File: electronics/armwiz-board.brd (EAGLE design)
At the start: 99.1 x 51.5 mm, 100 parts, among them J1 MICRO-SDCARD-CONNECTOR-330006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, J15 Cortex Debug, J16 ST-Link v2, J2 CORTEX_DEBUGSMD, U1 STM32F10XRXT6, U4 MIC5219-3.3V, X1 FH12-12S-1S, Y3 32.768kHz

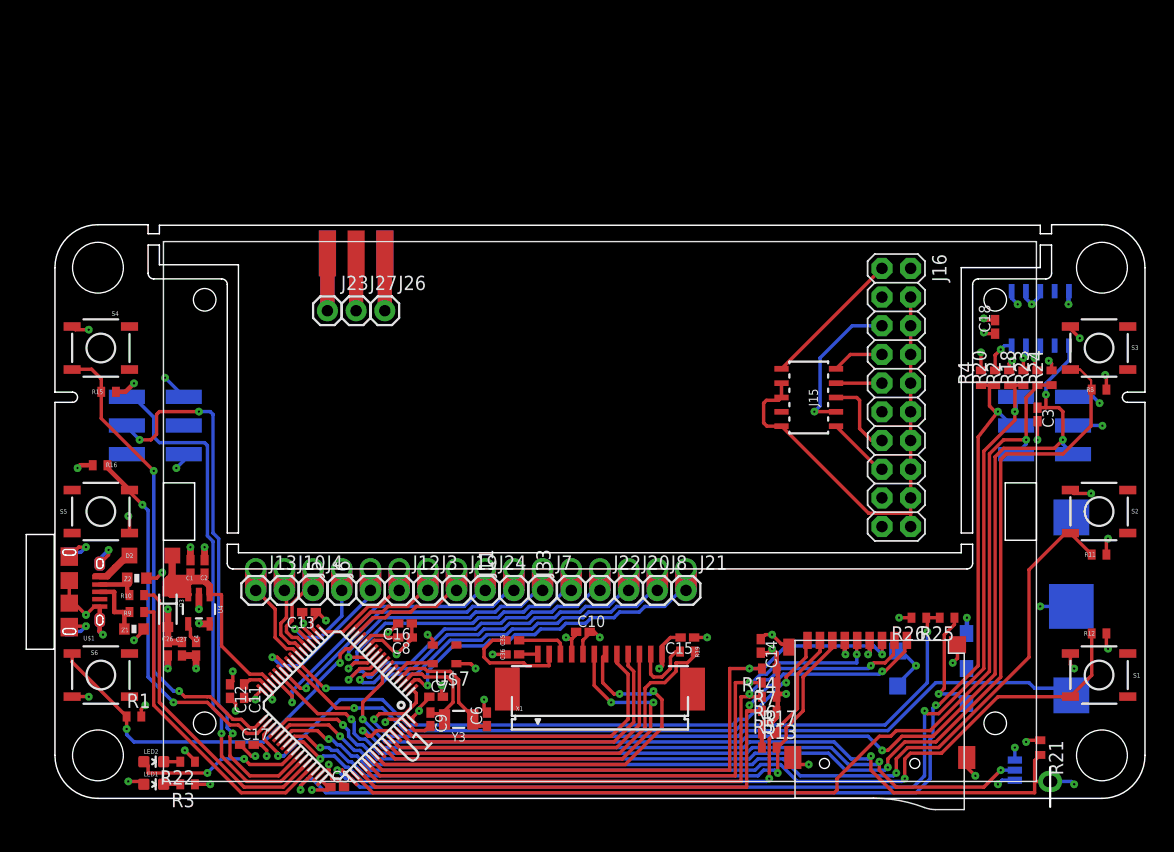
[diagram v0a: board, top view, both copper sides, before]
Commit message: Changed to a metric layout. Moved to a 7x2 2.0mm module connector.
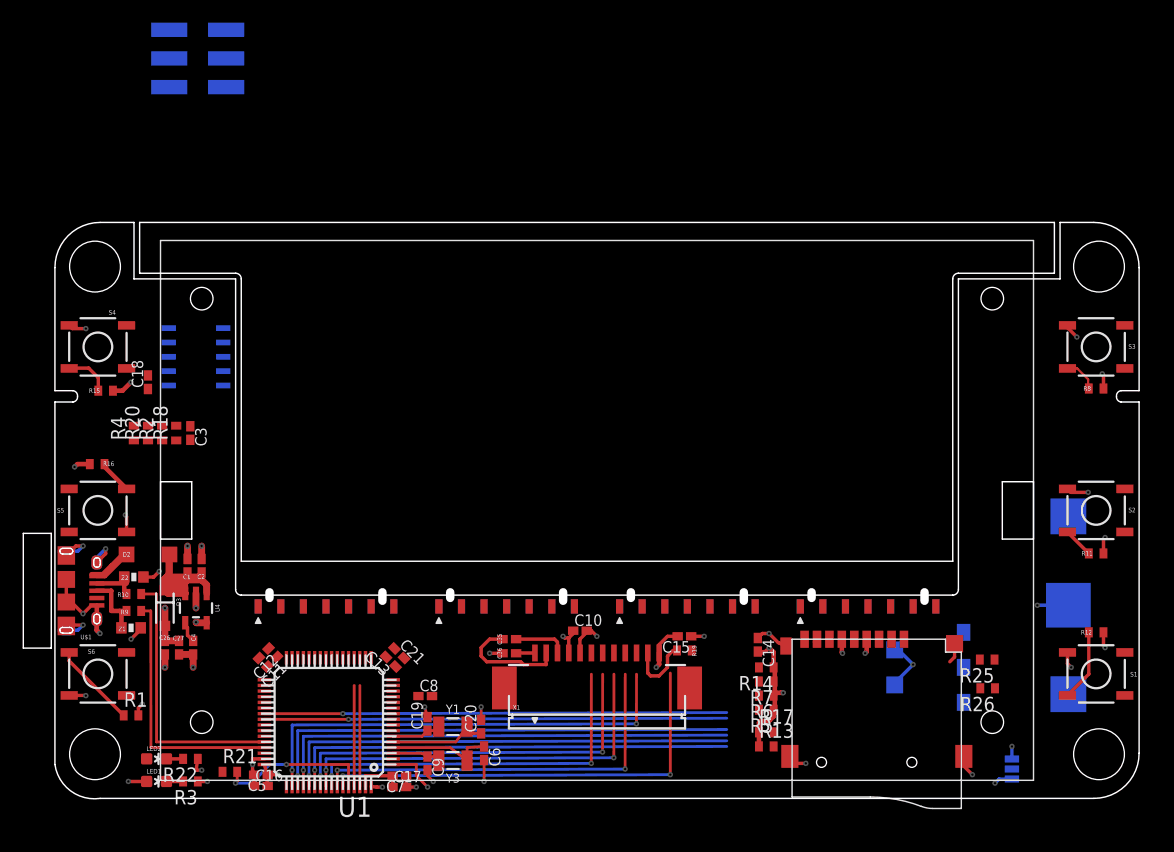
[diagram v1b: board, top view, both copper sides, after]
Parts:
- removed J$1: SMA_EDGE, SparkFun-Connectors:SMA-EDGE
- removed J10, J11, J12, J13, J19, J20, J21, J22, J23, J24, J26, J27, J3, J33, J4, J5, J6, J7, J8: (no value), SparkFun-Connectors:1X01
- removed J14: (no value), PaxInstruments-Connectors:CONNECTORS_2X3_SMT_POSTS_T400
- removed J15: Cortex Debug, SparkFun-Connectors:SAMTECH_FTSH-105-01
- removed J16: ST-Link v2, SparkFun-Connectors:2X10
- removed J17, J18: (no value), SparkFun-Connectors:1X01NS-KIT
- removed R23: 100R, resistor:R0402
- removed R24: 10K, resistor:R0402
- added C19, C20: 8pF, resistor:C0402K
- added C21: 10uF, resistor:C0402K
- added U$4, U$8, U$9: PAX_MODULE, PaxInstruments-Connectors:7X2_2MM_EDGE
- added Y1: 32.768kHz, SparkFun-FreqCtrl:CRYSTAL-SMD-3.2X1.5MM
- U$7: value ASDM1-16.000MHz-LCT -> PAX_MODULE; device crystal:ASE -> PaxInstruments-Connectors:7X2_2MM_EDGE
- moved U$6 117.1 mm to (78.0, 120.7)
- moved C18 75.2 mm to (8.24, 36.9)
- moved R18 75.2 mm to (10.7, 32.4)
- moved R2 75.2 mm to (9.49, 32.4)
- moved R20 75.2 mm to (8.24, 32.4)
- moved R4 75.2 mm to (6.99, 32.4)
- moved C3 75.0 mm to (12.0, 32.4)
- moved J2 74.8 mm to (12.5, 39.1), turned to 270 degrees
- moved R21 71.8 mm to (15.5, 2.35), turned to 0 degrees
- moved J25 32.7 mm to (12.6, 65.5)
- moved C16 19.2 mm to (18.2, 1.10), turned to 0 degrees
- moved C17 14.0 mm to (30.5, 1.00)
- moved R26 8.73 mm to (82.6, 9.75)
- moved C13 8.47 mm to (29.7, 12.1), turned to 135 degrees
- moved C7 7.72 mm to (30.5, 2.00), turned to 180 degrees
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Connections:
- net BOOT1 renamed (BOOT1)
- net MISO3 renamed PB4
- net MOSI3 renamed LCD_MOSI_(SPI3_MOSI)
- net RTC1 renamed RTC_OSC_IN
- net RTC2 renamed RTC_OSC_OUT
- net SCK3 renamed LCD_SCK_(SPI3_SCK)
- net SW_PWR renamed SW_PWR_(SYS_WKUP)
- removed net AD_GND: J15.3, J15.5, J15.9, J16.10, J16.12, J16.14, J16.16, J16.18, J16.20, J16.4, J16.6, J16.8
- removed net AD_NRST: J15.10, J16.15
- removed net AD_SWDCLK: J15.4, J16.9
- removed net AD_SWDIO: J15.2, J16.7
- removed net AD_SWO: J15.6, J16.13
- removed net AD_TDI: J15.8, J16.5
- removed net AD_VCC: J15.1, J16.1
- removed net LCD_A0: U1.62, X1.8
- removed net LCD_BL: R19.2, U1.58
- removed net LCD_CS: U1.59, X1.10
- removed net LCD_RST: U1.61, X1.9
- removed net MISO1: J10.1, U1.22
- removed net MOSI1: J13.1, U1.23
- removed net N$12: J2.6, R23.2
- removed net N$14: J$1.GND@1, J$1.GND@3, J26.1
- removed net N$15: J$1.GND@0, J$1.GND@2, J23.1
- removed net N$20: J$1.SIG, J27.1
- removed net PA2: J3.1, U1.16
- removed net PA3: J12.1, U1.17
- removed net PA4: J5.1, U1.20
- removed net PB10: J24.1, U1.29
- removed net PC0: J20.1, U1.8
- removed net PC1: J22.1, U1.9
- removed net PC13: J21.1, U1.2
- removed net SCLK1: J4.1, U1.21
- removed net SWDCLK: J14.2, R18.1, R2.1, U1.49
- removed net SWO: J14.6, R23.1, R24.1, U1.50
- removed net USB+: R9.2, U1.45
- removed net USB-: R10.2, U1.44
- removed net VBAT2: R25.2, R26.1, U1.25
- new net 12C1_SDA: U1.59
- new net CAN_RX: U$4.P$4, U$7.P$4, U$8.P$4, U$9.P$4, U1.61
- new net CAN_TX: U$4.P$6, U$7.P$6, U$8.P$6, U$9.P$6, U1.62
- new net GPIO_(SPI1_NSS): U$8.P$9, U1.20
- new net GPIO_(SPI2_NSS): U$4.P$9, U1.33
- new net I2C1_SCL: U$4.P$10, U$7.P$10, U1.58
- new net I2C1_SDA: U$4.P$8, U$7.P$8
- new net I2C2_SCL: U$8.P$10, U$9.P$10, U1.29
- new net I2C2_SDA: U$8.P$8, U$9.P$8, U1.30
- new net LCD_A0_(GPIO): U1.9, X1.8
- new net LCD_BL_(GPIO): R19.2, U1.8
- new net LCD_CS_(SPI3_NSS): U1.50, X1.10
- new net LCD_RST_(GPIO): U1.2, X1.9
- new net LED2: LED2.A
- new net N$51: U$8.P$11
- new net N$52: U$8.P$13
- new net N$57: U$4.P$11
- new net N$58: U$4.P$13
- new net N$68: U$7.P$9
- new net N$69: U$7.P$11
- new net N$70: U$7.P$13
- new net N$74: U$9.P$9
- new net N$75: U$9.P$11
- new net N$76: U$9.P$13
- new net OSC_OUT: C19.1, U1.6, Y1.P$1
- new net PC5: U1.25
- new net PC6: U1.37
- new net PC7: U1.38
- new net SPI1_MISO: U$8.P$5, U$9.P$5, U1.22
- new net SPI1_MOSI: U$8.P$3, U$9.P$3, U1.23
- new net SPI1_SCK: U$8.P$7, U$9.P$7, U1.21
- new net SPI2_MISO: U$4.P$5, U$7.P$5, U1.35
- new net SPI2_MOSI: U$4.P$3, U$7.P$3, U1.36
- new net SPI2_SCK: U$4.P$7, U$7.P$7, U1.34
- new net SWCLK: R18.1, R2.1, U1.49
- new net USART2_RX: U$4.P$12, U$7.P$12, U$8.P$12, U$9.P$12, U1.17
- new net USART2_TX: U$4.P$14, U$7.P$14, U$8.P$14, U$9.P$14, U1.16
- new net USB_DM: R10.2, U1.44
- new net USB_DP: R9.2, U1.45
- new net VBAT_1/2: R25.2, R26.1
- net 3.3V: now also C21.2, U$4.P$1, U$7.P$1, U$8.P$1, U$9.P$1; no longer J14.1, J18.1, R24.2, U$7.4
- net BOOT0: no longer J17.1
- net GND: now also C19.2, C20.2, C21.1, U$4.P$2, U$7.P$2, U$8.P$2, U$9.P$2; no longer J14.3, U$7.2
- net NRST: no longer J14.5
- net OSC_IN: now also C20.1, Y1.P$2; no longer U$7.3
- net PA1: no longer J19.1
- net PA8: no longer LED2.A
- net PB0: no longer J6.1
- net PB1: no longer J11.1
- net PC2: no longer J33.1
- net PC3: no longer J7.1
- net PC4: no longer J8.1
- net SD_DETECT: no longer U1.35
- net SWDIO: no longer J14.4
- net SW_A: no longer U1.36
- net SW_B: no longer U1.37
- net SW_C: no longer U1.38
- net SW_D: no longer U1.33
- net SW_E: no longer U1.34
- net VBUS: no longer U1.30
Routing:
- net NRST: track 104.8 -> 0.00 mm, vias 4 -> 0
- net SW_A: track 106.1 -> 3.07 mm, vias 2 -> 0
- net SWDIO: track 100.9 -> 0.00 mm, vias 3 -> 0
- net SWDCLK: track 96.4 -> 0.00 mm, vias 3 -> 0
- net SWO: track 92.8 -> 0.00 mm, vias 1 -> 0
- net SW_B: track 89.8 -> 2.69 mm, vias 2 -> 0
- net SW_C: track 83.0 -> 6.37 mm, vias 2 -> 0
- net (BOOT1): track 71.7 -> 0.00 mm, vias 3 -> 0
- net VBAT2: track 67.7 -> 0.00 mm, vias 2 -> 0
- net RTC_BAT: track 70.6 -> 4.46 mm
- net BOOT0: track 71.6 -> 13.7 mm
- net SD_DETECT: track 57.2 -> 0.00 mm, vias 2 -> 0
- net USART1_TX: track 48.9 -> 0.00 mm, vias 3 -> 0
- net USART1_RX: track 46.8 -> 0.00 mm, vias 1 -> 0
- net AD_GND: track 41.5 -> 0.00 mm
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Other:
- board size 99.1 x 51.5 mm -> 98.8 x 51 mm

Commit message: Updated board with new Pax Instruments library parts.
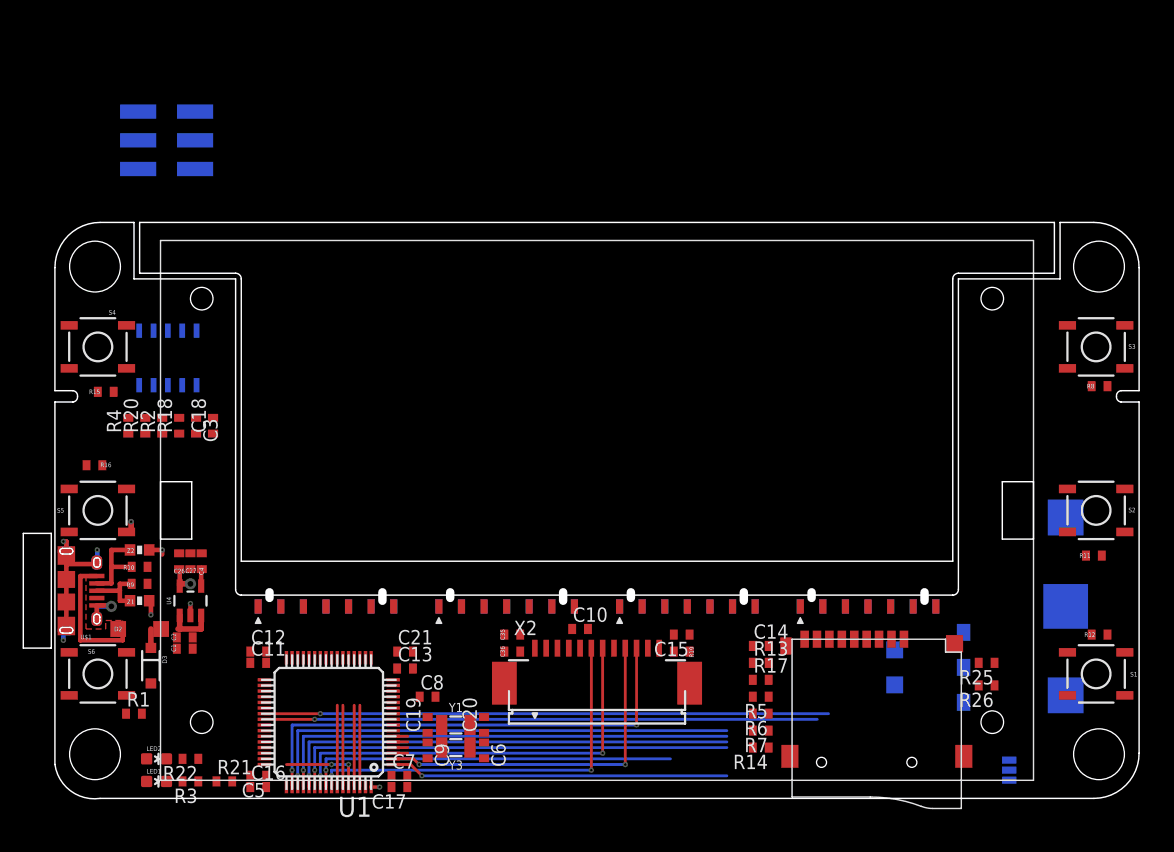
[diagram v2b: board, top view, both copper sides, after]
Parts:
- removed U$4, U$7, U$8, U$9: PAX_MODULE, PaxInstruments-Connectors:7X2_2MM_EDGE
- removed X1: FH12-12S-1S, PaxInstrument-T400:FH12-12S-1SH
- added MODULE1, MODULE2, MODULE3, MODULE4: PI-module-female, PaxInstruments-Connectors:M07X2_2MM_EDGE
- added X2: M12_BOTTOM_CONTACTS_FPC_1MM, PaxInstruments-Connectors:FPC_12P_1MM
- C1, C10, C11, C12, C13, C14, C15, C16, C17, C18, C19, C2, C20, C21, C26, C27, C3, C35, C36, C4, C5, C6, C7, C8, C9: device resistor:C0402K -> PaxInstruments-Capacitors:C0402
- J1: value MICRO-SDCARD-CONNECTOR-3300060P1 -> MICROSD; device PaxInstrument-T400:9P-SMD-W-RING -> PaxInstruments-Connectors:MICROSD_1
- R1, R11, R12, R15, R16, R8: value 10k -> 10K; device resistor:R0402 -> PaxInstruments-Resistors:R0402
- R10, R13, R14, R17, R18, R19, R2, R20, R21, R22, R25, R26, R3, R4, R5, R6, R7, R9: device resistor:R0402 -> PaxInstruments-Resistors:R0402
- moved U$6 59.8 mm to (81.3, 61.0)
- moved J25 7.75 mm to (9.89, 58.3)
- moved C26 7.75 mm to (11.0, 21.0), turned to 90 degrees
- moved C27 7.72 mm to (12.0, 21.0), turned to 90 degrees
- moved C4 7.69 mm to (13.0, 21.0), turned to 90 degrees
- moved R13 7.42 mm to (62.5, 12.0)
- moved C1 7.35 mm to (11.5, 13.2), turned to 0 degrees
- moved R14 7.12 mm to (62.5, 4.50)
- moved C18 6.93 mm to (14.0, 33.0)
- moved D2 6.64 mm to (7.50, 15.0)
- moved C2 6.52 mm to (11.5, 14.2), turned to 0 degrees
- moved D3 5.25 mm to (8.50, 11.8)
- moved R17 4.68 mm to (62.5, 10.5)
- moved R7 4.38 mm to (62.5, 6.00)
- moved Z1 2.52 mm to (7.50, 17.5)
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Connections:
- removed net 12C1_SDA: U1.59
- removed net N$52: U$8.P$13
- removed net N$58: U$4.P$13
- removed net N$70: U$7.P$13
- removed net N$76: U$9.P$13
- removed net PB4: U1.56
- new net PC0: U1.8
- net 3.3V: now also C11.1, C12.1, C13.1, C16.1, C17.1, C21.1, C26.2, C27.2, C8.1, MODULE1.P$1, MODULE2.P$1, MODULE3.P$1, MODULE4.P$1, R13.2, R14.2, R17.2, R5.2, R6.2, R7.2, X2.12, X2.5; no longer C11.2, C12.2, C13.2, C16.2, C17.2, C21.2, C26.1, C27.1, C8.2, R13.1, R14.1, R17.1, R5.1, R6.1, R7.1, U$4.P$1, U$7.P$1, U$8.P$1, U$9.P$1, X1.12, X1.5
- net CAN_RX: now also MODULE1.P$4, MODULE2.P$4, MODULE3.P$4, MODULE4.P$4; no longer U$4.P$4, U$7.P$4, U$8.P$4, U$9.P$4
- net CAN_TX: now also MODULE1.P$6, MODULE2.P$6, MODULE3.P$6, MODULE4.P$6; no longer U$4.P$6, U$7.P$6, U$8.P$6, U$9.P$6
- net GND: now also C1.1, C11.2, C12.2, C13.2, C16.2, C17.2, C2.1, C21.2, C26.1, C27.1, C8.2, MODULE1.P$13, MODULE1.P$2, MODULE2.P$13, MODULE2.P$2, MODULE3.P$13, MODULE3.P$2, MODULE4.P$13, MODULE4.P$2, R1.1, R22.2, R3.2, X2.4; no longer C1.2, C11.1, C12.1, C13.1, C16.1, C17.1, C2.2, C21.1, C26.2, C27.2, C8.1, R1.2, R22.1, R3.1, U$4.P$2, U$7.P$2, U$8.P$2, U$9.P$2, X1.4
- net GPIO_(SPI1_NSS): now also MODULE3.P$9; no longer U$8.P$9
- net GPIO_(SPI2_NSS): now also MODULE1.P$9; no longer U$4.P$9
- net I2C1_SCL: now also MODULE1.P$10, MODULE2.P$10; no longer U$4.P$10, U$7.P$10
- net I2C1_SDA: now also MODULE1.P$8, MODULE2.P$8, U1.59; no longer U$4.P$8, U$7.P$8
- net I2C2_SCL: now also MODULE3.P$10, MODULE4.P$10; no longer U$8.P$10, U$9.P$10
- net I2C2_SDA: now also MODULE3.P$8, MODULE4.P$8; no longer U$8.P$8, U$9.P$8
- net LCD_A0_(GPIO): now also X2.8; no longer X1.8
- net LCD_BL_(GPIO): now also U1.56; no longer U1.8
- net LCD_CS_(SPI3_NSS): now also X2.10; no longer X1.10
- net LCD_MOSI_(SPI3_MOSI): now also X2.6; no longer X1.6
- net LCD_RST_(GPIO): now also X2.9; no longer X1.9
- net LCD_SCK_(SPI3_SCK): now also X2.7; no longer X1.7
- net N$11: now also R22.1; no longer R22.2
- net N$37: now also X2.3; no longer X1.3
- net N$38: now also X2.2; no longer X1.2
- net N$39: now also X2.1; no longer X1.1
- net N$4: now also X2.11; no longer X1.11
- net N$51: now also MODULE3.P$11; no longer U$8.P$11
- net N$57: now also MODULE1.P$11; no longer U$4.P$11
- net N$68: now also MODULE2.P$9; no longer U$7.P$9
- net N$69: now also MODULE2.P$11; no longer U$7.P$11
- net N$7: now also R3.1; no longer R3.2
- net N$74: now also MODULE4.P$9; no longer U$9.P$9
- net N$75: now also MODULE4.P$11; no longer U$9.P$11
- net SDIO_CLK: now also R7.1; no longer R7.2
- net SDIO_CMD: now also R14.1; no longer R14.2
- net SDIO_D0: now also R13.1; no longer R13.2
- net SDIO_D1: now also R17.1; no longer R17.2
- net SDIO_D2: now also R5.1; no longer R5.2
- net SDIO_D3: now also R6.1; no longer R6.2
- net SPI1_MISO: now also MODULE3.P$5, MODULE4.P$5; no longer U$8.P$5, U$9.P$5
- net SPI1_MOSI: now also MODULE3.P$3, MODULE4.P$3; no longer U$8.P$3, U$9.P$3
- net SPI1_SCK: now also MODULE3.P$7, MODULE4.P$7; no longer U$8.P$7, U$9.P$7
- net SPI2_MISO: now also MODULE1.P$5, MODULE2.P$5; no longer U$4.P$5, U$7.P$5
- net SPI2_MOSI: now also MODULE1.P$3, MODULE2.P$3; no longer U$4.P$3, U$7.P$3
- net SPI2_SCK: now also MODULE1.P$7, MODULE2.P$7; no longer U$4.P$7, U$7.P$7
- net SW_PWR_(SYS_WKUP): now also R1.2; no longer R1.1
- net USART2_RX: now also MODULE1.P$12, MODULE2.P$12, MODULE3.P$12, MODULE4.P$12; no longer U$4.P$12, U$7.P$12, U$8.P$12, U$9.P$12
- net USART2_TX: now also MODULE1.P$14, MODULE2.P$14, MODULE3.P$14, MODULE4.P$14; no longer U$4.P$14, U$7.P$14, U$8.P$14, U$9.P$14
- net VBUS: now also C1.2, C2.2; no longer C1.1, C2.1
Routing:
- net GND: track 78.3 -> 24.3 mm, vias 35 -> 8
- net 3.3V: track 44.7 -> 3.35 mm, vias 18 -> 2
- net 12C1_SDA: track 38.9 -> 0.00 mm, vias 2 -> 0
- net PB4: track 35.3 -> 0.00 mm, vias 2 -> 0
- net LCD_BL_(GPIO): track 0.00 -> 33.0 mm, vias 0 -> 1
- net LCD_RST_(GPIO): track 0.01 -> 31.1 mm, vias 0 -> 2
- net I2C1_SCL: track 35.3 -> 7.20 mm, vias 2 -> 0
- net RTC_BAT: track 4.46 -> 30.0 mm
- net USB_DM: track 24.0 -> 0.00 mm
- net USB_DP: track 23.0 -> 0.00 mm
- net VBUS: track 25.4 -> 6.12 mm
- net N$38: track 10.1 -> 0.00 mm
- net SDIO_D0: track 41.1 -> 50.0 mm
- net RTC_OSC_OUT: track 9.59 -> 1.30 mm
- net SDIO_D1: track 41.3 -> 49.0 mm
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- added copper zone on layer 1, net VBUS_IN

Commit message: Signals routed to the module headers.
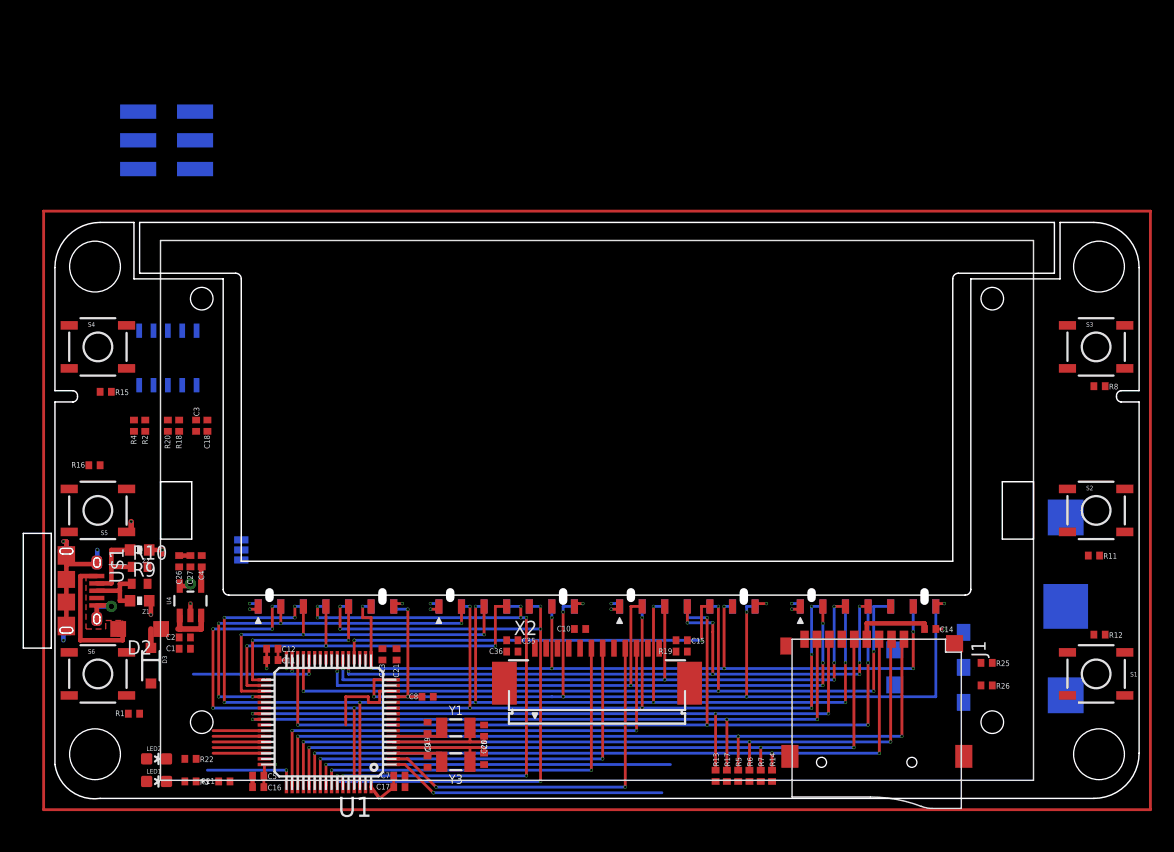
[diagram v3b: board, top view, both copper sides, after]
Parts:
- C1, C12, C16, C17, C19, C20, C21, C26, C35, C36, C4, C6, C9: device PaxInstruments-Capacitors:C0402 -> PaxInstruments-RCL:0402
- C10, C11, C13, C14, C15, C18, C2, C27, C3, C5, C7, C8: value 0.1uF -> 100nF; device PaxInstruments-Capacitors:C0402 -> PaxInstruments-RCL:0402
- R1, R11, R12, R13, R14, R15, R16, R17, R18, R19, R2, R20, R21, R22, R25, R26, R3, R4, R5, R6, R7, R8: device PaxInstruments-Resistors:R0402 -> PaxInstruments-RCL:0402
- moved SJ2 70.7 mm to (16.5, 22.0)
- moved C14 15.1 mm to (77.5, 15.0), turned to 180 degrees
- moved R13 10.8 mm to (58.5, 2.00), turned to 270 degrees
- moved R17 9.01 mm to (59.5, 2.00), turned to 270 degrees
- moved R5 7.28 mm to (60.5, 2.00), turned to 270 degrees
- moved R6 5.59 mm to (61.5, 2.00), turned to 270 degrees
- moved R7 4.00 mm to (62.5, 2.00), turned to 270 degrees
- moved R14 2.69 mm to (63.5, 2.00), turned to 270 degrees
- moved C13 2.36 mm to (29.0, 12.8), turned to 90 degrees
- moved R20 2.00 mm to (10.0, 33.0)
- moved R2 1.50 mm to (8.00, 33.0)
- moved C11 1.27 mm to (19.2, 12.2), turned to 180 degrees
- moved C12 1.27 mm to (19.2, 13.2), turned to 180 degrees
- moved Y3 1.25 mm to (35.5, 3.25)
- moved C9 1.00 mm to (33.0, 3.25)
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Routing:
- net GND: track 24.3 -> 338.1 mm, vias 8 -> 19
- net CAN_TX: track 7.20 -> 105.2 mm, vias 0 -> 11
- net CAN_RX: track 7.20 -> 104.2 mm, vias 0 -> 12
- net USART2_TX: track 0.00 -> 88.0 mm, vias 0 -> 7
- net I2C2_SDA: track 0.00 -> 79.2 mm, vias 0 -> 5
- net USART2_RX: track 0.00 -> 73.2 mm, vias 0 -> 8
- net I2C2_SCL: track 0.00 -> 70.7 mm, vias 0 -> 5
- net SPI1_SCK: track 0.00 -> 61.7 mm, vias 0 -> 7
- net SPI1_MOSI: track 0.00 -> 60.5 mm, vias 0 -> 5
- net SPI1_MISO: track 0.00 -> 59.5 mm, vias 0 -> 5
- net I2C1_SCL: track 7.20 -> 56.5 mm, vias 0 -> 6
- net I2C1_SDA: track 7.20 -> 53.7 mm, vias 0 -> 7
- net GPIO_(SPI1_NSS): track 0.00 -> 36.0 mm, vias 0 -> 2
- net SPI2_SCK: track 0.00 -> 35.0 mm, vias 0 -> 3
- net SPI2_MOSI: track 0.00 -> 35.0 mm, vias 0 -> 5
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- added copper zone on layer 16, net GND
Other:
- outline, holes or cut-outs redrawn
